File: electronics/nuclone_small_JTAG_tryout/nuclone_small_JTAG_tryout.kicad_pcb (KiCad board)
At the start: 2 copper layers, 50 x 50 mm, 54 parts, among them J3 nuclone_small_left, J4 nuclone_small_right, J5 FTDI_PINS_1X06, J6 DevBoardUartInput

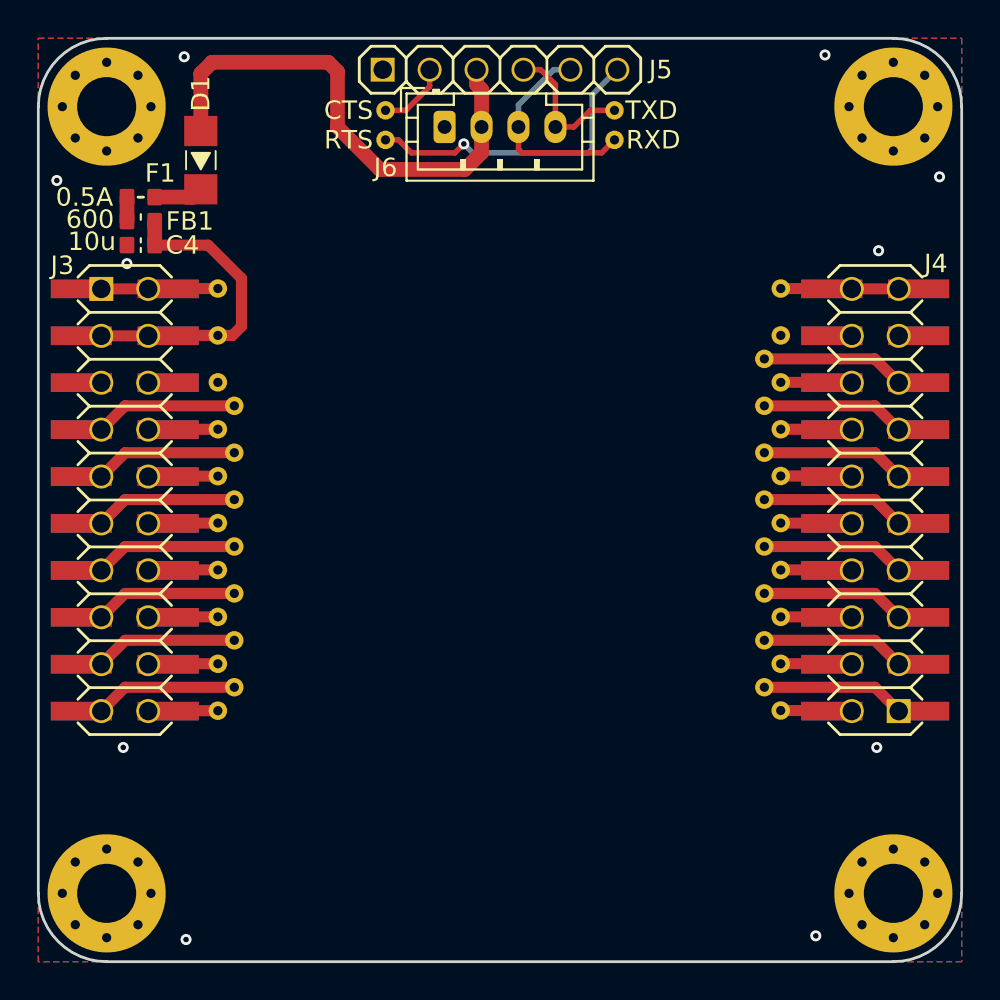
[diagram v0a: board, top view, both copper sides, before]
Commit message: WIP schematic entry: added reset control/detection and power control/detection
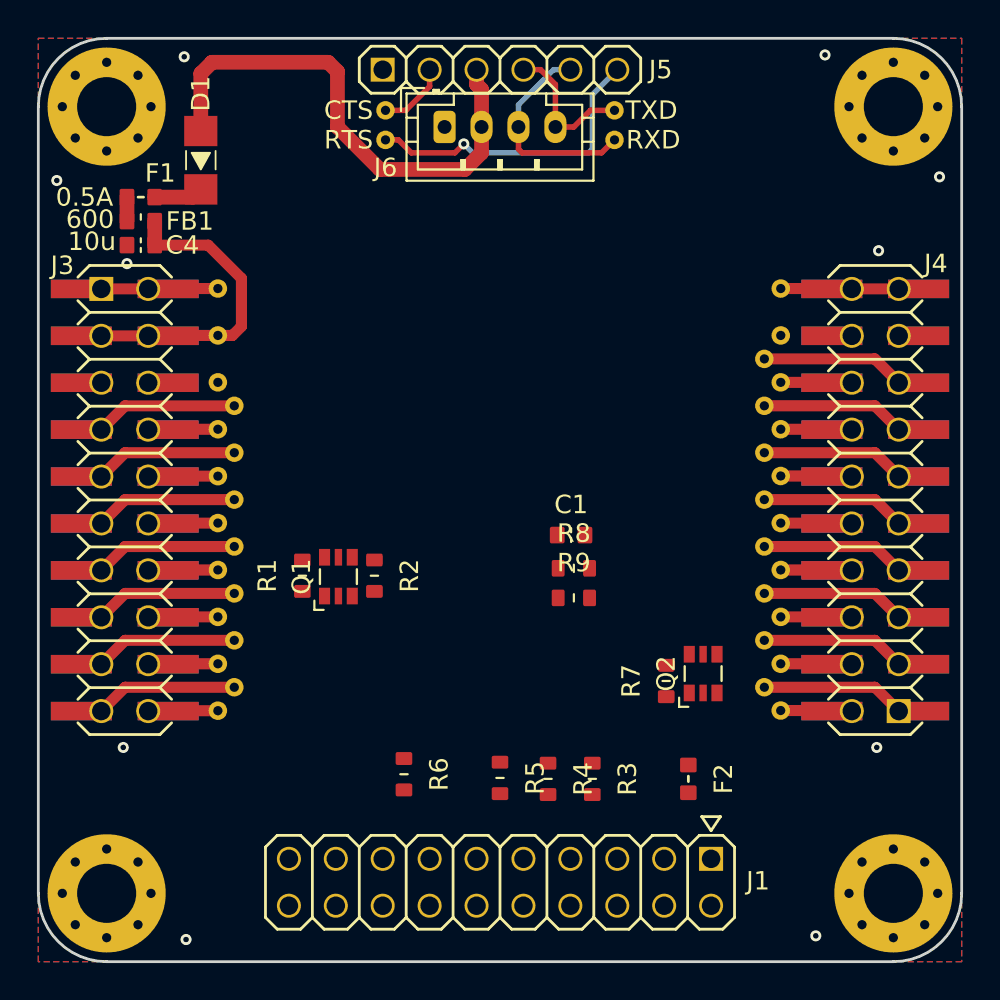
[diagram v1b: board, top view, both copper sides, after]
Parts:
- added C1: 1uF, SquantorRcl:C_0603, F.Cu at (88.8, 87.9)
- added F2: 300mA, SquantorRcl:F_0603_hand, F.Cu at (95.2, 101.1)
- added J1: SEGGER_2X10_OUT, SquantorConnectors:Header-0254-2X10-H010, F.Cu at (85.0, 106.7)
- added Q1: BSD840, SquantorIC:SOT363-NXP-hand, F.Cu at (76.2, 90.2)
- added Q2: NTJD4152, SquantorIC:SOT363-NXP-hand, F.Cu at (96.0, 95.4)
- added R1: 10K, SquantorRcl:R_0603_hand, F.Cu at (74.3, 90.1)
- added R2: 10K, SquantorRcl:R_0603_hand, F.Cu at (78.2, 90.1)
- added R3: 100, SquantorRcl:R_0603_hand, F.Cu at (90.0, 101.1)
- added R4: 100, SquantorRcl:R_0603_hand, F.Cu at (87.6, 101.1)
- added R5: 100, SquantorRcl:R_0603_hand, F.Cu at (85.0, 101.0)
- added R6: 100, SquantorRcl:R_0603_hand, F.Cu at (79.8, 100.8)
- added R7: 10K, SquantorRcl:R_0603_hand, F.Cu at (94.0, 95.8)
- added R8: 10K, SquantorRcl:R_0603_hand, F.Cu at (89.0, 89.7)
- added R9: 10K, SquantorRcl:R_0603_hand, F.Cu at (89.0, 91.3)
- N2: value V20230714 -> V20230801
